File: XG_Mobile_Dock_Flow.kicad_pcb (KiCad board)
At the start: 4 copper layers, 220 x 65 mm, 109 parts, among them J1 5-1775443-8, J10 SWD, J11 UART, J12 I2C1, J13 39300240, J14 469911008, J17 8730, J2 20455-040E-76, J3 20455-040E-76, J4 3-2362375-4, J5 USB_C_Receptacle, Q16 AO3401A, Q17 2N7002W, SW1 SW_Push, U1 DS160PR410RNQR, U12 STM32F030C8Tx, U2 DS160PR410RNQR

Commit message: fixed part numbers
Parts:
- C27, C28, C29, C30: value 0.1μF -> 100nF

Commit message: fixed pcie 8 power connector part number
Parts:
- J14: value 469911008 -> 455860005
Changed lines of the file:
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@@
 			)
 		)
-		(property "Value" "469911008"
+		(property "Value" "455860005"
 			(at -1.849998 3.5 0)
 			(unlocked yes)
@@
 			)
 		)
-		(property "Part_Number" "469911008"
+		(property "Part_Number" "455860005"
 			(at 0 0 180)
 			(unlocked yes)
@@
 			)
 		)
-		(property "LCSC" "C17470577"
+		(property "LCSC" "C17693884"
 			(at 0 0 180)
 			(unlocked yes)

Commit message: updated part number for molex with latest one
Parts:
- J13: value 39300240 -> 39301240
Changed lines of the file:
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@@
 			)
 		)
-		(property "Value" "39300240"
+		(property "Value" "39301240"
 			(at -2.2 3.4 0)
 			(unlocked yes)
@@
 			)
 		)
-		(property "Part_Number" "39300240"
+		(property "Part_Number" "39301240"
 			(at 0 0 180)
 			(unlocked yes)
@@
 			)
 		)
-		(property "LCSC" "C492361"
+		(property "LCSC" "C492347"
 			(at 0 0 180)
 			(unlocked yes)

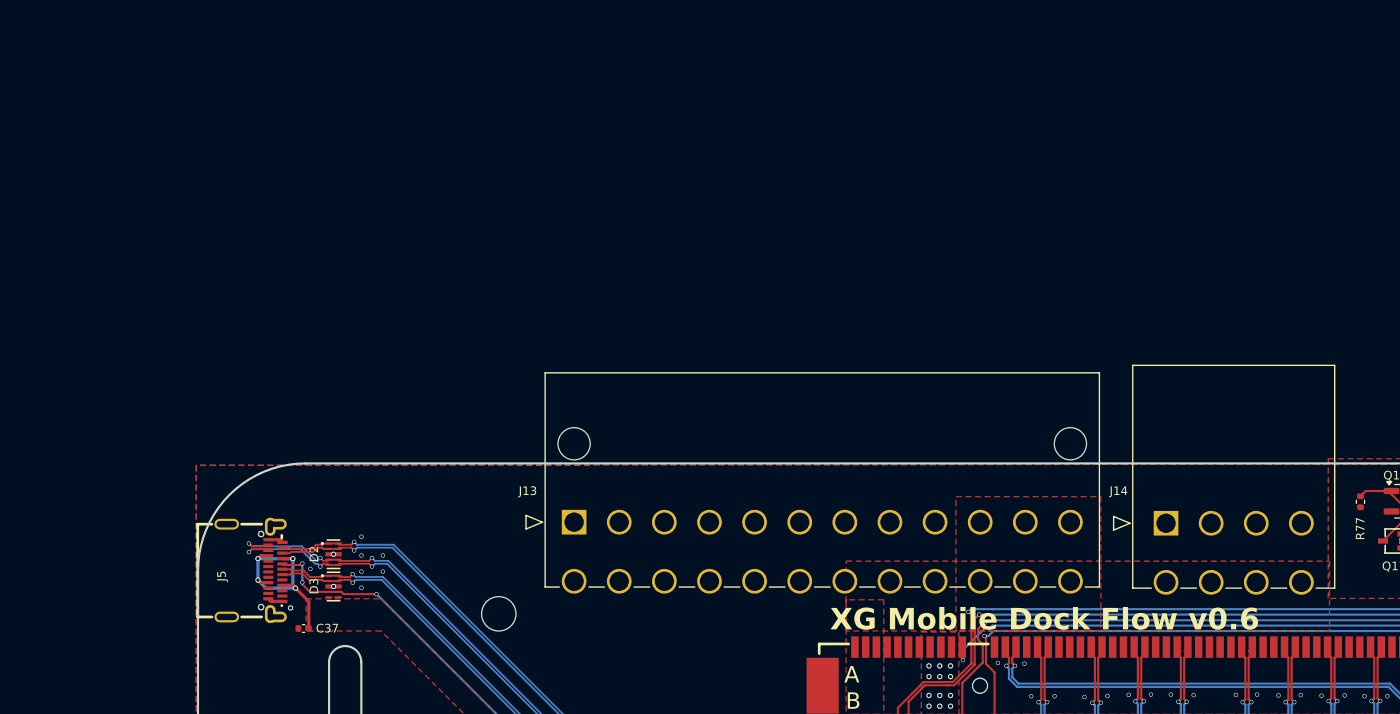
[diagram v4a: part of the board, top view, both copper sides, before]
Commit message: updated flow version with proper design
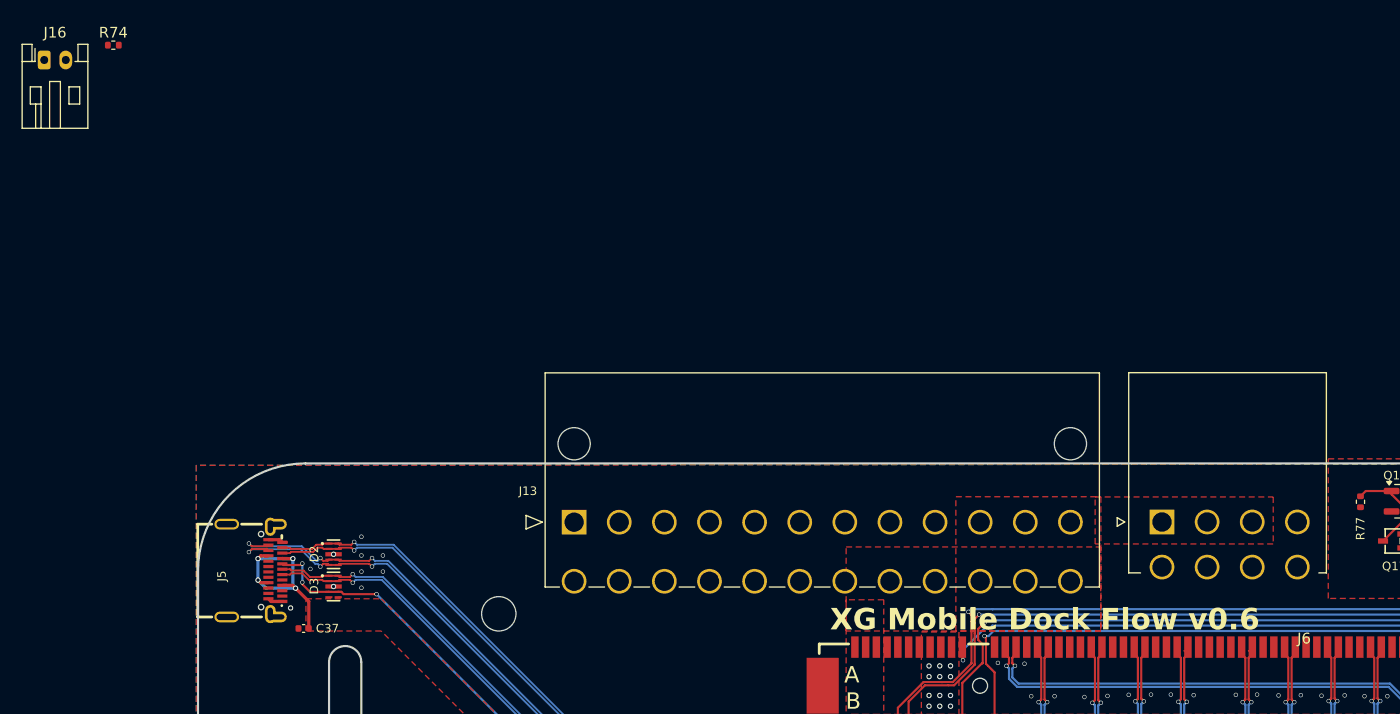
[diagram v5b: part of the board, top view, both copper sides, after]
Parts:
- removed J14: 455860005, 469911008:CON_469911008
- added J16: ~, Connector_JST:JST_PH_S2B-PH-K_1x02_P2.00mm_Horizontal, F.Cu at (2.48, 1.88)
- added J6: 455860005, 455860005:MOLEX_455860005, F.Cu at (106.5, 44.9)
- added R74: 47k, Resistor_SMD:R_0402_1005Metric, F.Cu at (8.90, 0.49)
